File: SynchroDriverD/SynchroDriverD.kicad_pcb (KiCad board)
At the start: 2 copper layers, 100 x 100 mm, 207 parts, among them J1 SYNC, J2 POWER, J3 ROLL, J4 PITCH, J5 YAW, J6 NEEDLES, J7 FLAG, Q1 SIS990, Q10 MMBTA42, Q11 MMBTA92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

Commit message: Complete layout
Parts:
- moved R77 0.17 mm to (114.0, 126.5)
- moved R70 0.15 mm to (159.0, 129.6)
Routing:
- net +3.3V: track 0.00 -> 359.1 mm, vias 0 -> 6
- net /PWM_YE: track 1.40 -> 111.8 mm, vias 0 -> 4
- net /PWM_YR: track 1.40 -> 109.1 mm, vias 0 -> 4
- net /PWM_PR: track 1.40 -> 106.3 mm, vias 0 -> 4
- net /PWM_RE: track 1.40 -> 104.6 mm, vias 0 -> 4
- net GND: track 17.2 -> 118.9 mm, vias 9 -> 75
- net /Pots/OUT4: track 0.00 -> 82.4 mm, vias 0 -> 2
- net /Pots/OUT1: track 0.00 -> 79.4 mm, vias 0 -> 1
- net /PWM_RR: track 1.40 -> 75.6 mm, vias 0 -> 2
- net /PWM_PE: track 1.40 -> 74.3 mm, vias 0 -> 4
- net /PWM_Y0: track 0.00 -> 67.9 mm, vias 0 -> 4
- net /Pots/OUT5: track 0.00 -> 65.7 mm, vias 0 -> 2
- net /PWM_Y1: track 0.00 -> 64.9 mm, vias 0 -> 4
- net /FlagDriver/OUT: track 0.00 -> 64.2 mm, vias 0 -> 3
- net /Pots/OUT2: track 0.00 -> 63.7 mm, vias 0 -> 2
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- added copper zone on B.Cu, net +12V
- added copper zone on B.Cu, net +36V
- added copper zone on F.Cu, net +36V
- added copper zone on B.Cu, net +5V
- added copper zone on B.Cu, net -12V
- added copper zone on B.Cu, net GND
- added copper zone on F.Cu, net GND
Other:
- board text added: "+12V"
- board text added: "+30V"
- board text added: "-12V"
- board text added: "5V"
- board text added: "APOLLO FDAI DRIVER BOARD"
- board text added: "GND"
- board text added: "PITCH A"
- board text added: "PITCH B"
- board text added: "PITCH C"
- board text added: "REF IN"
- board text added: "ROLL A"
- board text added: "ROLL B"
- board text added: "ROLL C"
- board text added: "TEENSY GOES HERE"
- board text added: "TUBE TIME 2025"
- board text added: "YAW A"
- board text added: "YAW B"
- board text added: "YAW C"

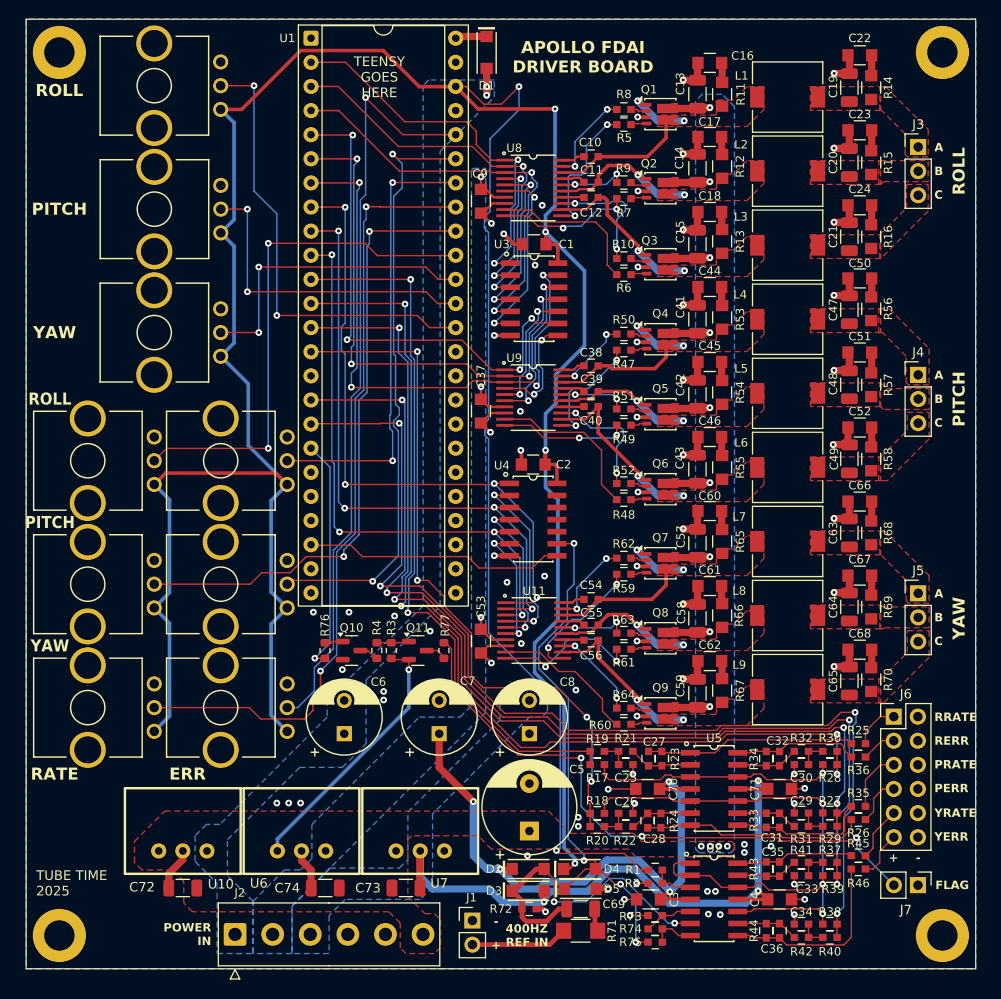
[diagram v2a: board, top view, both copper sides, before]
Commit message: Improve ref in, clearance for 115V
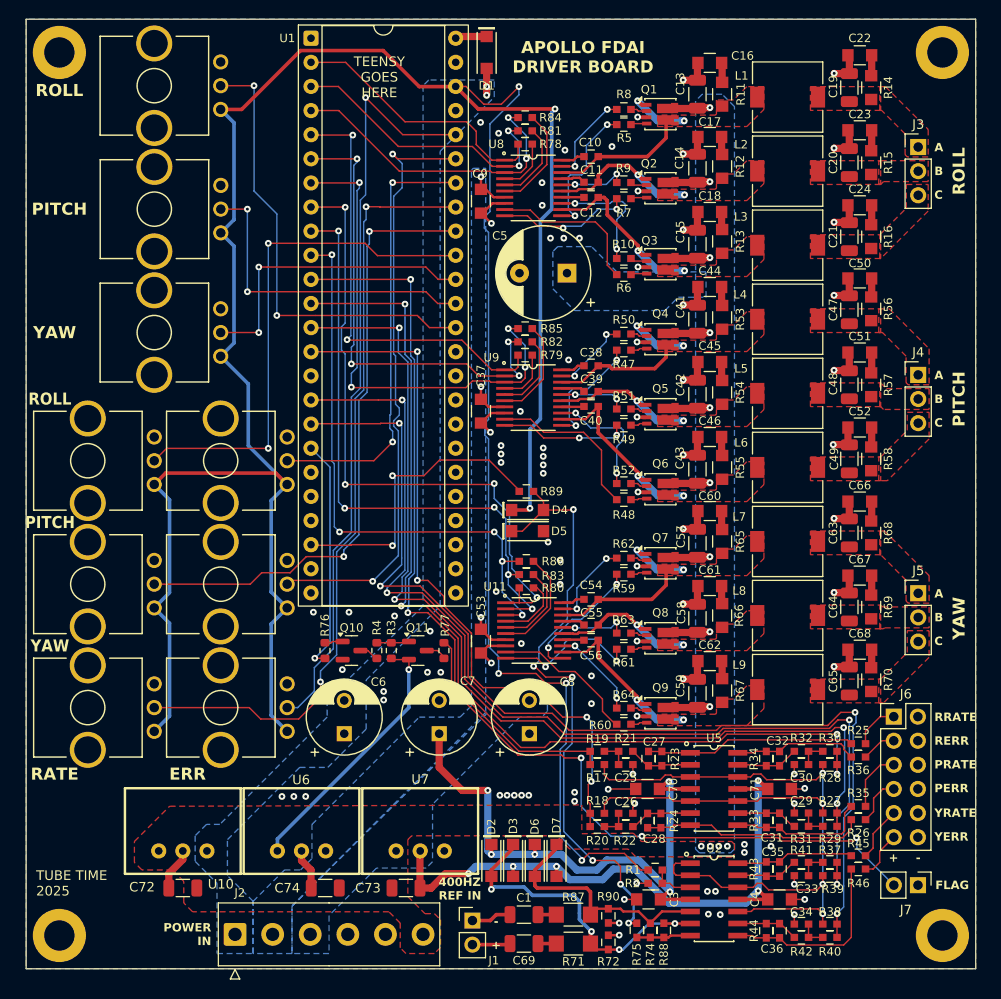
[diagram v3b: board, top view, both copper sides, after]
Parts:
- removed C2: 1uF, Passive:CAPC2012X55
- removed R73: 1K, Passive:RESC1608X55
- removed U3, U4: 74LV14, Active:SOP127P620X175-14
- added D6: SS320LWH, Active:SOD3716X117, F.Cu at (123.6, 148.6)
- added D7: SS320LWH, Active:SOD3716X117, F.Cu at (125.9, 148.6)
- added R78: 0, Passive:RESC1608X55, F.Cu at (122.6, 73.2)
- added R79: 0, Passive:RESC1608X55, F.Cu at (122.6, 95.4)
- added R80: 0, Passive:RESC1608X55, F.Cu at (122.7, 119.9)
- added R81: 0, Passive:RESC1608X55, F.Cu at (122.6, 71.8)
- added R82: 0, Passive:RESC1608X55, F.Cu at (122.6, 94.0)
- added R83: 0, Passive:RESC1608X55, F.Cu at (122.7, 118.5)
- added R84: 0, Passive:RESC1608X55, F.Cu at (122.6, 70.4)
- added R85: 0, Passive:RESC1608X55, F.Cu at (122.6, 92.6)
- added R86: 0, Passive:RESC1608X55, F.Cu at (122.7, 117.1)
- added R87: 10K, Passive:RESC3216X70, F.Cu at (127.6, 154.3)
- added R88: 22K, Passive:RESC1608X55, F.Cu at (137.2, 156.0)
- added R89: 4.7K, Passive:RESC1608X55, F.Cu at (122.7, 109.7)
- added R90: 1K, Passive:RESC1608X55, F.Cu at (131.3, 154.4)
- C1: value 1uF -> 10uF; footprint Passive:CAPC2012X55 -> Capacitor_SMD:C_1206_3216Metric
- R71: value 1K -> 10K
- R72: value 100K -> 1K
- R74: value 1MEG -> DNI
- U11, U8, U9: value DRV8300 -> DRV8300DI
- moved C1 70.6 mm to (122.4, 154.3), turned to 0 degrees
- moved C5 56.3 mm to (124.5, 86.7), turned to 180 degrees
- moved D4 38.2 mm to (122.8, 111.7)
- moved D5 38.1 mm to (122.8, 113.9)
- moved R72 9.06 mm to (131.3, 157.2), turned to 90 degrees
- moved C69 7.00 mm to (122.4, 157.4), turned to 0 degrees
- moved D2 3.98 mm to (119.0, 148.6), turned to -90 degrees
- moved D3 3.58 mm to (121.3, 148.6), turned to -90 degrees
- moved R75 2.30 mm to (134.3, 156.0), turned to -90 degrees
- moved R71 1.55 mm to (127.6, 157.4)
- moved R74 0.54 mm to (135.7, 156.0), turned to 90 degrees
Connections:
- C1 pad 1: +3.3V -> /InputComparator/INN
- C1 pad 2: GND -> Net-(C1-Pad2)
- C69 pad 1: Net-(C69-Pad1) -> /InputComparator/INP
- C69 pad 2: Net-(D2-A) -> Net-(C69-Pad2)
- J1 pad 1: GND -> /InputComparator/INN
- J1 pad 2: /InputComparator/IN -> /InputComparator/INP
- R71 pad 1: /InputComparator/IN -> Net-(C69-Pad2)
- R71 pad 2: Net-(C69-Pad1) -> Net-(D2-A)
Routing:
- net +3.3V: track 359.1 -> 310.6 mm
- net Net-(D6-A): track 5.21 -> 24.8 mm
- net Net-(U11-INLA): track 20.0 -> 7.19 mm, vias 2 -> 0
- net /PWM_R0: track 40.5 -> 28.4 mm, vias 2 -> 0
- net /PWM_R2: track 44.3 -> 32.6 mm
- net /PWM_R1: track 41.8 -> 30.6 mm
- net /InputComparator/IN: track 10.2 -> 0.00 mm
- net Net-(U8-INLB): track 18.1 -> 8.72 mm, vias 2 -> 0
- net GND: track 118.9 -> 109.7 mm, vias 75 -> 95
- net Net-(U8-INLA): track 14.8 -> 5.81 mm, vias 2 -> 0
- net Net-(U8-INLC): track 20.1 -> 11.2 mm, vias 2 -> 0
- net /PWM_P2: track 61.4 -> 52.8 mm
- net Net-(D4-A): track 56.3 -> 64.4 mm, vias 4 -> 6
- net /PWM_P0: track 54.7 -> 46.9 mm, vias 4 -> 2
- net Net-(U11-INLB): track 16.6 -> 9.24 mm, vias 2 -> 0
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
